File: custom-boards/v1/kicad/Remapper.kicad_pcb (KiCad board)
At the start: 2 copper layers, 25 x 35 mm, 57 parts, among them SW102 SW_Push, SW2 SW_Push, U103 RP2040, U105 W25Q128JVS, U3 RP2040, U4 TLV73333PDBV, U5 W25Q128JVS, Y1 Crystal_GND24, Y101 Crystal_GND24

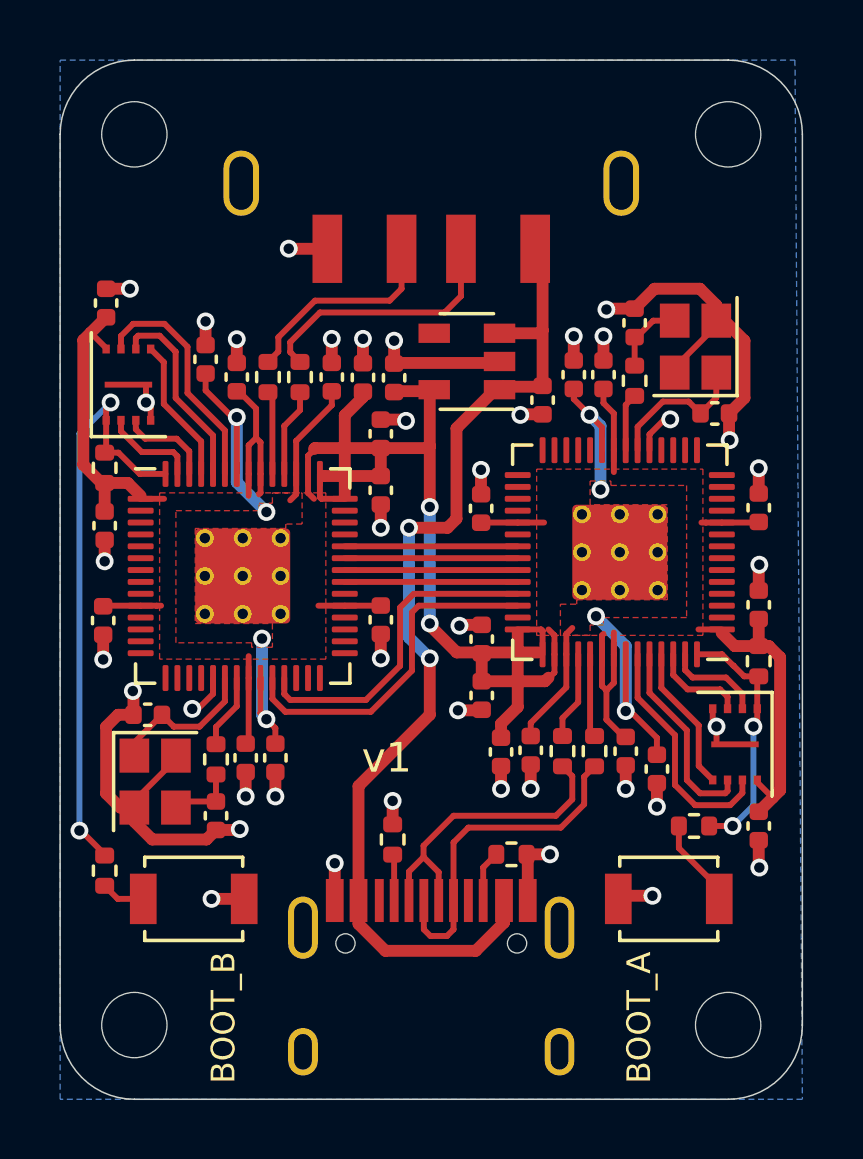
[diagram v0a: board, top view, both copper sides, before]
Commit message: Update custom boards
This commit makes the following changes to the custom PCB designs.

v1-v5: flash chip footprint changed, previous one caused issues in
manufacturing. Some other components moved around as a result.

v1-v5: flash chip changed from 1 megabyte to 2 megabyte one.

v1: USB Type A port component changed, previous one was consistently
soldered on crooked by JLCPCB.

The new designs are named v1.1-v5.1.

Schematics and enclosure files are unchanged.
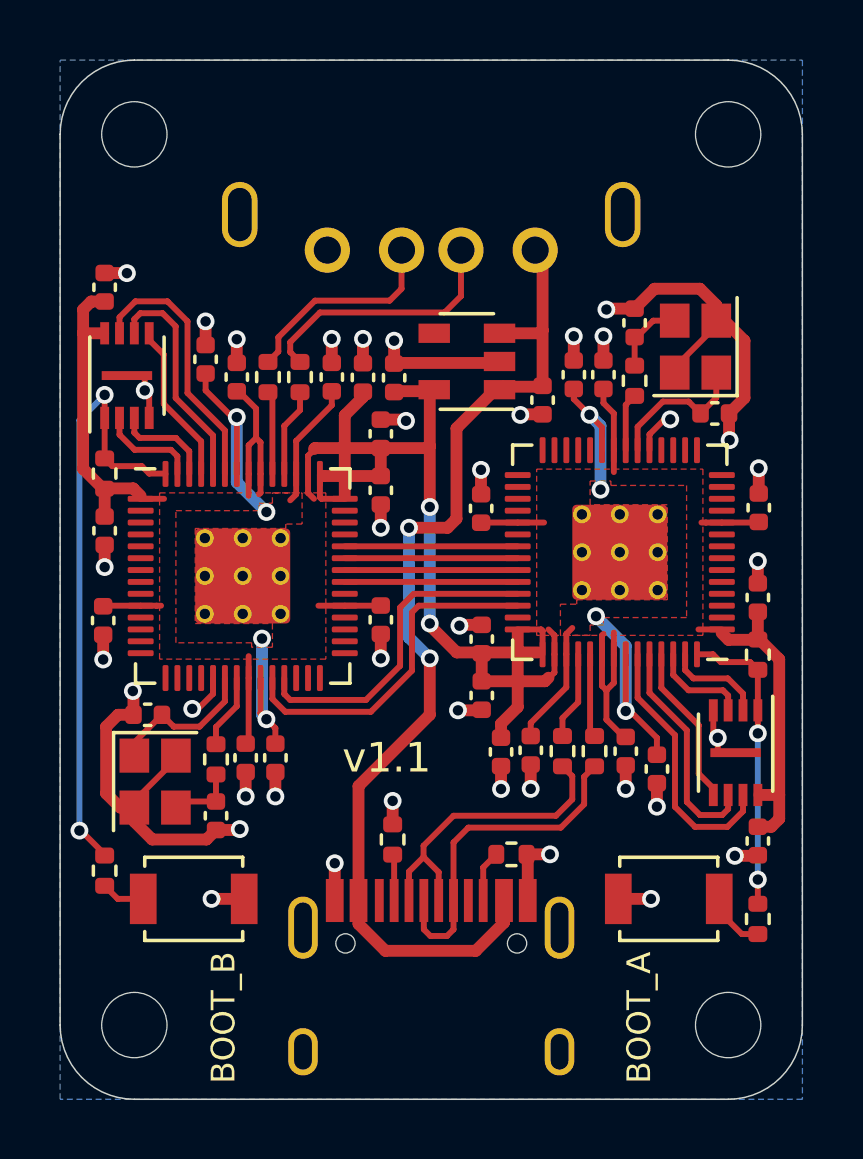
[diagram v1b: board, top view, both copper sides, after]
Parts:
- C118, C119, C18, C19: value 30p -> 15p
- U4: footprint Package_TO_SOT_SMD:SOT-23-5 -> SOT:SOT-23-5
- USB1: footprint Type-A:908-261A2021S10100 -> Type-A:C42459
- moved USB101 5.04 mm to (142.0, 62.0)
- moved R106 3.80 mm to (153.0, 59.9), turned to -90 degrees
- moved USB1 0.55 mm to (142.0, 36.8)
- moved C17 0.53 mm to (131.0, 38.6)
- moved C117 0.51 mm to (153.0, 57.3)
- moved U5 0.31 mm to (131.8, 41.6)
- moved U105 0.28 mm to (152.2, 54.3)
- moved C104 0.25 mm to (153.0, 49.1)
- moved R105 0.22 mm to (153.0, 51.0)
- moved R5 0.19 mm to (131.0, 44.9)
- moved C4 0.17 mm to (131.0, 46.9)
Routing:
- net 1QSPI_SS: track 8.58 -> 10.1 mm
- net +3V3: track 84.3 -> 85.7 mm
- net GND: track 61.8 -> 60.7 mm, vias 40 -> 39
- net QSPI_SD3: track 7.97 -> 8.99 mm
- net QSPI_SCLK: track 6.61 -> 7.62 mm
- net 1QSPI_SD3: track 8.08 -> 9.00 mm
- net 1QSPI_SCLK: track 6.72 -> 7.62 mm
- net Net-(R106-Pad2): track 2.89 -> 2.04 mm
- net QSPI_SD0: track 4.91 -> 5.46 mm
- net 1QSPI_SD0: track 4.95 -> 5.46 mm
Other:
- board text added: "v1.1"
- board text removed: "v1"
